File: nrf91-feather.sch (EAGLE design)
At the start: 88 parts, among them J2 CON-HEADER-1X12-MALE-PIN, J3 CON-HEADER-1X16-MALE-PIN, J4 CON-1909763-1, J5 CON-SIM-104224-0820, J6 CON-S2B-PH-SM4-TB(LF)(SN), J7 CON-1909763-1, J8 CON-USB-DX07S016JA1R1500, J9 CON-TC2030-MCP-NL, Q1 MOSFET-P-SC89, Q2 MOSFET-DUAL-COMP-SOT563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

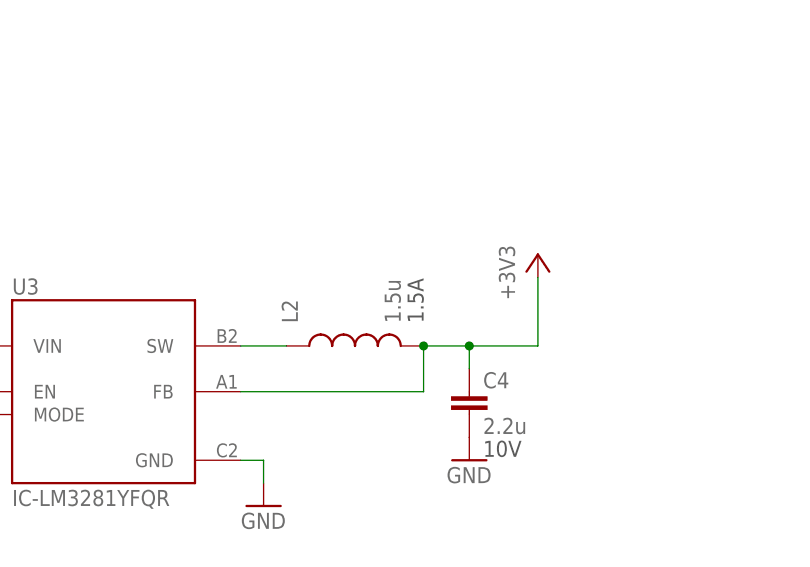
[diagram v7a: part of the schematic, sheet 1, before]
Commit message: Latest changes to nRF91
Changed:
* Power supply inductor
* Power supply tests board updated
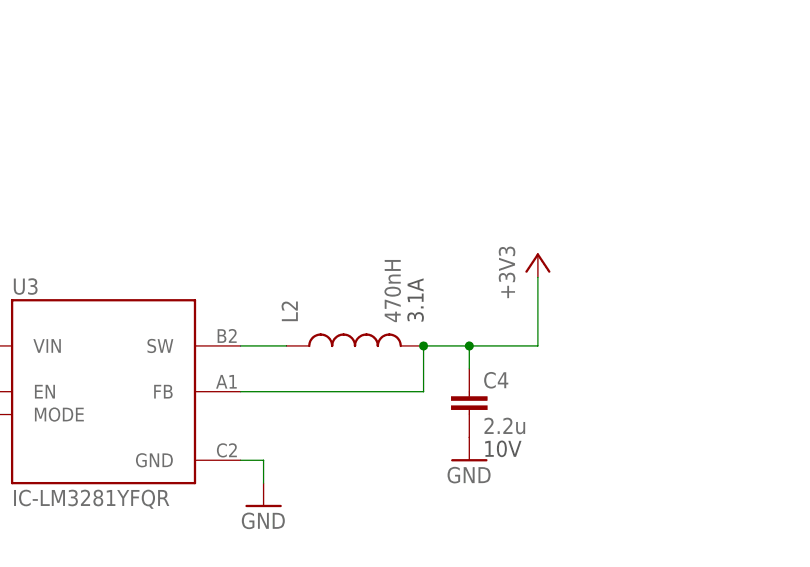
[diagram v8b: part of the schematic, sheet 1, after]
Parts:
- L2: value 1.5u -> 470nH; device wolff-den:IND-1.5U-1.5A-2X2 -> wolff-den:IND-3.1A-60MOHM-0805
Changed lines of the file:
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@@
 <part name="P+2" library="wolff-den" library_urn="urn:adsk.eagle:library:6370453" deviceset="VBUS" device=""/>
 <part name="P+4" library="wolff-den" library_urn="urn:adsk.eagle:library:6370453" deviceset="VSYS" device=""/>
-<part name="L2" library="wolff-den" library_urn="urn:adsk.eagle:library:6370453" deviceset="IND" device="" package3d_urn="urn:adsk.eagle:package:5807324/5" technology="-1.5U-1.5A-2X2" value="1.5u"/>
+<part name="L2" library="wolff-den" library_urn="urn:adsk.eagle:library:6370453" deviceset="IND" device="-0805" package3d_urn="urn:adsk.eagle:package:29902828/3" technology="-3.1A-60MOHM" value="470nH"/>
 <part name="C4" library="wolff-den" library_urn="urn:adsk.eagle:library:6370453" deviceset="CAP" device="-0603" package3d_urn="urn:adsk.eagle:package:5807321/7" technology="-2.2U-10V-01" value="2.2u"/>
 <part name="GND19" library="supply1" library_urn="urn:adsk.eagle:library:371" deviceset="GND" device=""/>
